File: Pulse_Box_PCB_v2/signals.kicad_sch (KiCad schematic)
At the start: 30 parts, among them J2 Conn_01x11, J3 Conn_01x11, J4 Conn_01x03, J5 Conn_01x03, J6 Conn_01x03_Pin, P1 USB_C_Plug_USB2.0, SW1 SW_Push, SW2 SW_Push, U1 ESP32-S3-WROOM-1, U2 USBLC6-2SC6, U4 SN74LV1T34DBV, U5 74LVC1G3157, U6 SN74LV1T34DBV

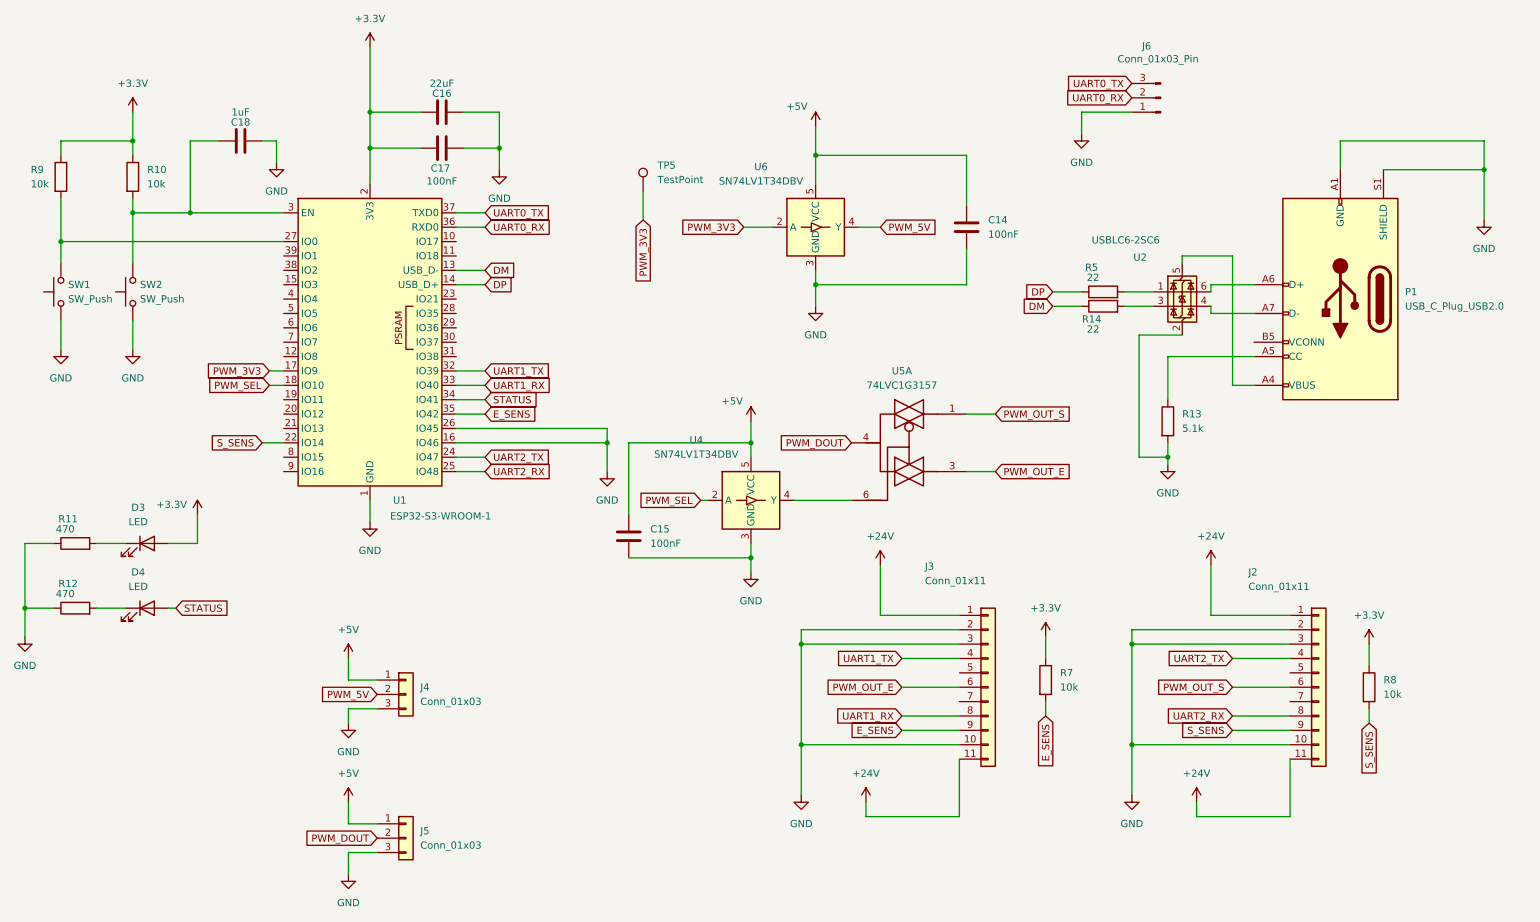
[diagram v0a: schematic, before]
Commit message: complete v2 and v1 panel design, this is the final design sent to jlcpcb for v2
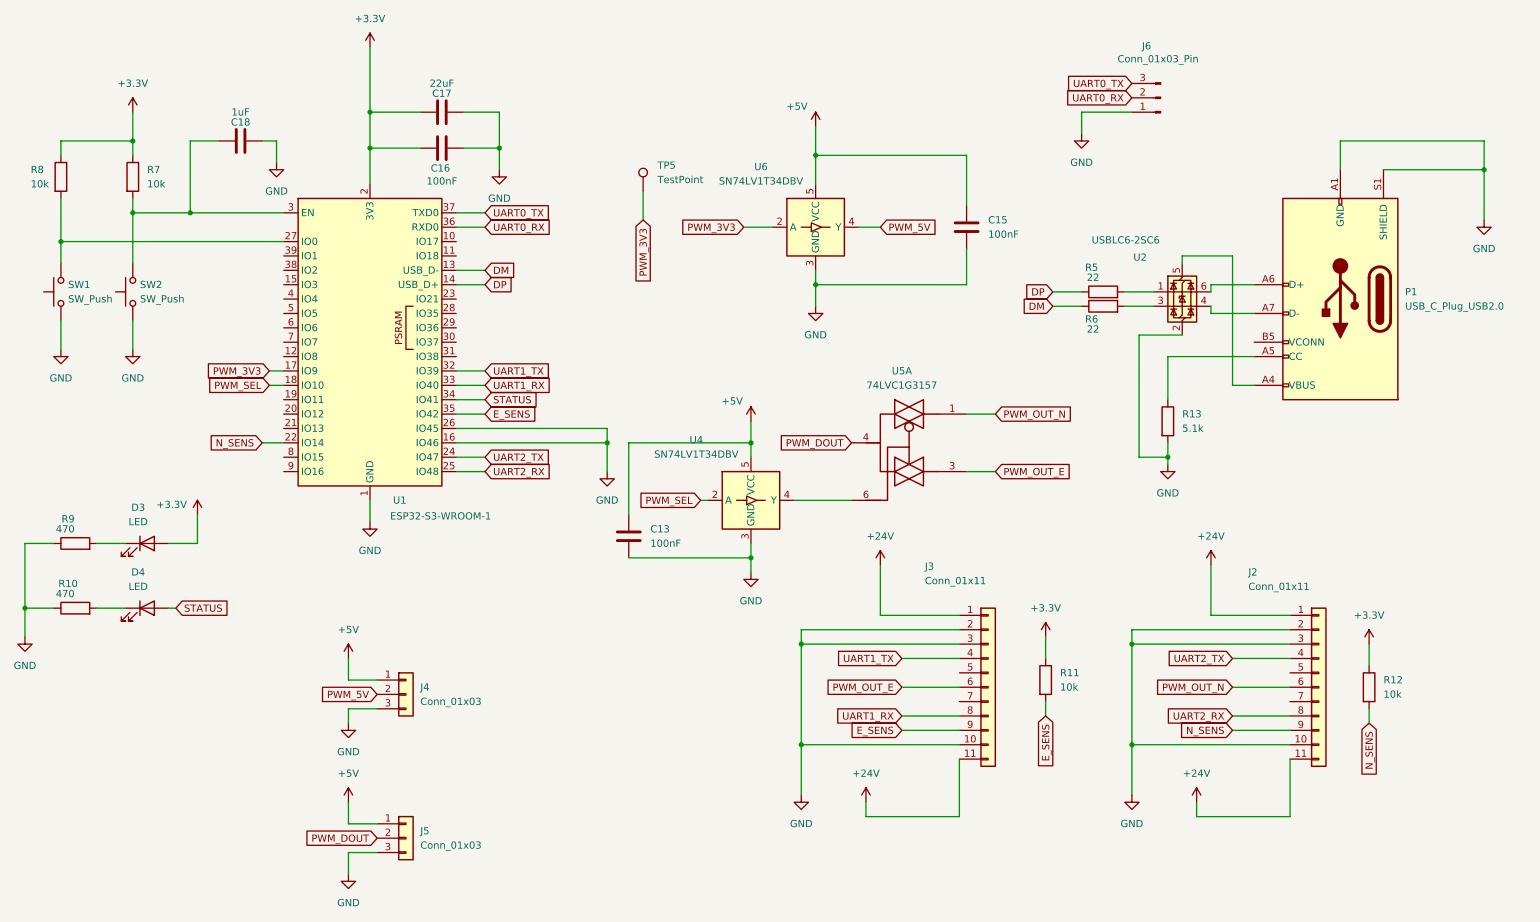
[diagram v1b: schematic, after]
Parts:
- C18: footprint Capacitor_SMD:C_0603_1608Metric -> Capacitor_SMD:C_0402_1005Metric
- J4, J5: footprint Connector_JST:JST_PH_S3B-PH-SM4-TB_1x03-1MP_P2.00mm_Horizontal -> Connector_JST:JST_PH_B3B-PH-K_1x03_P2.00mm_Vertical; JLCPCB Part # C265101 -> C131339
- renumbered C15 to C13, C14 to C15, C17 to C16, C16 to C17, R12 to R10, R7 to R11, R8 to R12, R14 to R6, R10 to R7, R9 to R8, R11 to R9
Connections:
- net PWM_OUT_S renamed PWM_OUT_N
- net S_SENS renamed N_SENS
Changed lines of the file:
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@@
 		)
 	)
-	(global_label "PWM_OUT_S"
+	(global_label "PWM_OUT_N"
 		(shape input)
 		(at 189.23 85.09 0)
@@
 		)
 		(property "Intersheetrefs" "${INTERSHEET_REFS}"
-			(at 203.1613 85.09 0)
+			(at 203.2823 85.09 0)
 			(effects
 				(font
@@
 		)
 	)
-	(global_label "UART0_RX"
+	(global_label "N_SENS"
 		(shape input)
-		(at 99.06 52.07 0)
+		(at 255.27 139.7 270)
 		(fields_autoplaced yes)
 		(effects
@@
 				(size 1.27 1.27)
 			)
-			(justify left)
+			(justify right)
 		)
 		(property "Intersheetrefs" "${INTERSHEET_REFS}"
-			(at 111.3585 52.07 0)
+			(at 255.27 149.8818 90)
 			(effects
 				(font
 					(size 1.27 1.27)
 				)
-				(justify left)
+				(justify right)
 				(hide yes)
 			)
 		)
 	)
-	(global_label "PWM_3V3"
+	(global_label "UART0_RX"
 		(shape input)
-		(at 144.78 52.07 180)
+		(at 99.06 52.07 0)
 		(fields_autoplaced yes)
 		(effects
@@
 				(size 1.27 1.27)
 			)
-			(justify right)
+			(justify left)
 		)
 		(property "Intersheetrefs" "${INTERSHEET_REFS}"
-			(at 133.1468 52.07 0)
+			(at 111.3585 52.07 0)
 			(effects
 				(font
 					(size 1.27 1.27)
 				)
-				(justify right)
+				(justify left)
 				(hide yes)
 			)
 		)
 	)
-	(global_label "S_SENS"
+	(global_label "PWM_3V3"
 		(shape input)
-		(at 59.69 90.17 180)
+		(at 144.78 52.07 180)
 		(fields_autoplaced yes)
 		(effects
@@
 		)
 		(property "Intersheetrefs" "${INTERSHEET_REFS}"
-			(at 49.6292 90.17 0)
+			(at 133.1468 52.07 0)
 			(effects
 				(font
@@
 		)
 	)
-	(global_label "S_SENS"
+	(global_label "N_SENS"
 		(shape input)
-		(at 255.27 139.7 270)
+		(at 59.69 90.17 180)
 		(fields_autoplaced yes)
 		(effects
@@
 		)
 		(property "Intersheetrefs" "${INTERSHEET_REFS}"
-			(at 255.27 149.7608 90)
+			(at 49.5082 90.17 0)
 			(effects
 				(font
@@
 		)
 	)
-	(global_label "UART2_RX"
+	(global_label "N_SENS"
 		(shape input)
-		(at 231.14 138.43 180)
+		(at 231.14 140.97 180)
 		(fields_autoplaced yes)
 		(effects
@@
 		)
 		(property "Intersheetrefs" "${INTERSHEET_REFS}"
-			(at 218.8415 138.43 0)
+			(at 220.9582 140.97 0)
 			(effects
 				(font
@@
 		)
 	)
-	(global_label "UART0_TX"
+	(global_label "UART2_RX"
 		(shape input)
-		(at 99.06 49.53 0)
+		(at 231.14 138.43 180)
 		(fields_autoplaced yes)
 		(effects
@@
 				(size 1.27 1.27)
 			)
-			(justify left)
+			(justify right)
 		)
 		(property "Intersheetrefs" "${INTERSHEET_REFS}"
-			(at 111.0561 49.53 0)
+			(at 218.8415 138.43 0)
 			(effects
 				(font
 					(size 1.27 1.27)
 				)
-				(justify left)
+				(justify right)
 				(hide yes)
 			)
 		)
 	)
-	(global_label "S_SENS"
+	(global_label "UART0_TX"
 		(shape input)
-		(at 231.14 140.97 180)
+		(at 99.06 49.53 0)
 		(fields_autoplaced yes)
 		(effects
@@
 				(size 1.27 1.27)
 			)
-			(justify right)
+			(justify left)
 		)
 		(property "Intersheetrefs" "${INTERSHEET_REFS}"
-			(at 221.0792 140.97 0)
+			(at 111.0561 49.53 0)
 			(effects
 				(font
 					(size 1.27 1.27)
 				)
-				(justify right)
+				(justify left)
 				(hide yes)
 			)
 		)
 	)
-	(global_label "PWM_OUT_S"
+	(global_label "PWM_OUT_N"
 		(shape input)
 		(at 231.14 133.35 180)
@@
 		)
 		(property "Intersheetrefs" "${INTERSHEET_REFS}"
-			(at 217.2087 133.35 0)
+			(at 217.0877 133.35 0)
 			(effects
 				(font
@@
 		(dnp no)
 		(fields_autoplaced yes)
-		(property "Reference" "R10"
+		(property "Reference" "R7"
 			(at 39.37 41.9099 0)
 			(effects
@@
 			(project ""
 				(path "/ef0e555f-a8f1-4b4b-84db-9e9da0748d24/9cdbe47c-d654-4511-bc17-02ce4a145abd"
-					(reference "R10")
+					(reference "R7")
 					(unit 1)
 				)
@@
 			)
 		)
-		(property "Footprint" "Capacitor_SMD:C_0603_1608Metric"
+		(property "Footprint" "Capacitor_SMD:C_0402_1005Metric"
 			(at 52.07 37.7952 0)
 			(effects
@@
 		(on_board yes)
 		(dnp no)
-		(property "Reference" "R12"
+		(property "Reference" "R10"
 			(at 25.4 115.062 90)
 			(effects
@@
 			(project "Pulse_Box_PCB_v2"
 				(path "/ef0e555f-a8f1-4b4b-84db-9e9da0748d24/9cdbe47c-d654-4511-bc17-02ce4a145abd"
-					(reference "R12")
+					(reference "R10")
 					(unit 1)
 				)
@@
 		(on_board yes)
 		(dnp no)
-		(property "Reference" "R8"
+		(property "Reference" "R12"
 			(at 257.81 132.0799 0)
 			(effects
@@
 			(project "Pulse_Box_PCB_v2"
 				(path "/ef0e555f-a8f1-4b4b-84db-9e9da0748d24/9cdbe47c-d654-4511-bc17-02ce4a145abd"
-					(reference "R8")
+					(reference "R12")
 					(unit 1)
 				)
@@
 		(on_board yes)
 		(dnp no)
-		(property "Reference" "C16"
+		(property "Reference" "C17"
 			(at 91.44 28.448 90)
 			(effects
@@
 			(project ""
 				(path "/ef0e555f-a8f1-4b4b-84db-9e9da0748d24/9cdbe47c-d654-4511-bc17-02ce4a145abd"
-					(reference "C16")
+					(reference "C17")
 					(unit 1)
 				)
@@
 		(dnp no)
 		(fields_autoplaced yes)
-		(property "Reference" "C15"
+		(property "Reference" "C13"
 			(at 128.27 105.4099 0)
 			(effects
@@
 			(project "Pulse_Box_PCB_v2"
 				(path "/ef0e555f-a8f1-4b4b-84db-9e9da0748d24/9cdbe47c-d654-4511-bc17-02ce4a145abd"
-					(reference "C15")
+					(reference "C13")
 					(unit 1)
 				)
@@
 		(on_board yes)
 		(dnp no)
-		(property "Reference" "R11"
+		(property "Reference" "R9"
 			(at 25.4 103.632 90)
 			(effects
@@
 			(project "Pulse_Box_PCB_v2"
 				(path "/ef0e555f-a8f1-4b4b-84db-9e9da0748d24/9cdbe47c-d654-4511-bc17-02ce4a145abd"
-					(reference "R11")
+					(reference "R9")
 					(unit 1)
 				)
@@
 			)
 		)
-		(property "Footprint" "Connector_JST:JST_PH_S3B-PH-SM4-TB_1x03-1MP_P2.00mm_Horizontal"
+		(property "Footprint" "Connector_JST:JST_PH_B3B-PH-K_1x03_P2.00mm_Vertical"
 			(at 85.09 160.02 0)
 			(effects
@@
 			)
 		)
-		(property "JLCPCB Part #" "C265101"
+		(property "JLCPCB Part #" "C131339"
 			(at 85.09 160.02 0)
 			(effects
@@
 		(dnp no)
 		(fields_autoplaced yes)
-		(property "Reference" "R7"
+		(property "Reference" "R11"
 			(at 200.66 130.8099 0)
 			(effects
@@
 			(project ""
 				(path "/ef0e555f-a8f1-4b4b-84db-9e9da0748d24/9cdbe47c-d654-4511-bc17-02ce4a145abd"
-					(reference "R7")
+					(reference "R11")
 					(unit 1)
 				)
@@
 		(on_board yes)
 		(dnp no)
-		(property "Reference" "R9"
+		(property "Reference" "R8"
 			(at 18.796 41.91 0)
 			(effects
@@
 			(project "Pulse_Box_PCB_v2"
 				(path "/ef0e555f-a8f1-4b4b-84db-9e9da0748d24/9cdbe47c-d654-4511-bc17-02ce4a145abd"
-					(reference "R9")
+					(reference "R8")
 					(unit 1)
 				)
@@
 		(on_board yes)
 		(dnp no)
-		(property "Reference" "C17"
+		(property "Reference" "C16"
 			(at 91.186 41.656 90)
 			(effects
@@
 			(project "Pulse_Box_PCB_v2"
 				(path "/ef0e555f-a8f1-4b4b-84db-9e9da0748d24/9cdbe47c-d654-4511-bc17-02ce4a145abd"
-					(reference "C17")
+					(reference "C16")
 					(unit 1)
 				)
@@
 		(on_board yes)
 		(dnp no)
-		(property "Reference" "R14"
+		(property "Reference" "R6"
 			(at 206.248 68.326 90)
 			(effects
@@
 			(project "Pulse_Box_PCB_v2"
 				(path "/ef0e555f-a8f1-4b4b-84db-9e9da0748d24/9cdbe47c-d654-4511-bc17-02ce4a145abd"
-					(reference "R14")
+					(reference "R6")
 					(unit 1)
 				)
@@
 			)
 		)
-		(property "Footprint" "Connector_JST:JST_PH_S3B-PH-SM4-TB_1x03-1MP_P2.00mm_Horizontal"
+		(property "Footprint" "Connector_JST:JST_PH_B3B-PH-K_1x03_P2.00mm_Vertical"
 			(at 85.09 134.62 0)
 			(effects
@@
 			)
 		)
-		(property "JLCPCB Part #" "C265101"
+		(property "JLCPCB Part #" "C131339"
 			(at 85.09 134.62 0)
 			(effects
@@
 		(dnp no)
 		(fields_autoplaced yes)
-		(property "Reference" "C14"
+		(property "Reference" "C15"
 			(at 187.96 50.7999 0)
 			(effects
@@
 			(project "Pulse_Box_PCB_v2"
 				(path "/ef0e555f-a8f1-4b4b-84db-9e9da0748d24/9cdbe47c-d654-4511-bc17-02ce4a145abd"
-					(reference "C14")
+					(reference "C15")
 					(unit 1)
 				)
